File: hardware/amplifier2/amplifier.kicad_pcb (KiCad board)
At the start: 2 copper layers, 95 x 82 mm, 132 parts, among them IC1 AD8331, IC2 ISL55210, IC3 LP38798, IC4 NC7SVU04, IC5 LTC2252, J1 0, M1 MountingHole_3.2mm_M3_Pad, M2 MountingHole_3.2mm_M3_Pad, M3 MountingHole_3.2mm_M3_Pad, M4 MountingHole_3.2mm_M3_Pad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

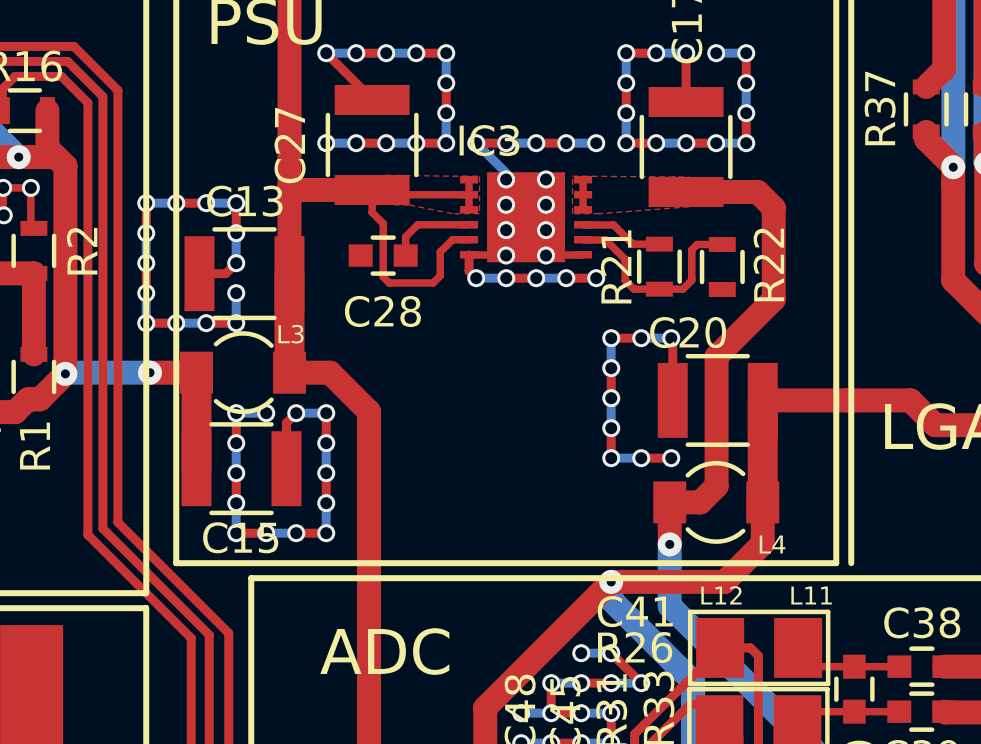
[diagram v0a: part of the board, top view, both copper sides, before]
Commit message: fixed wrong footprint
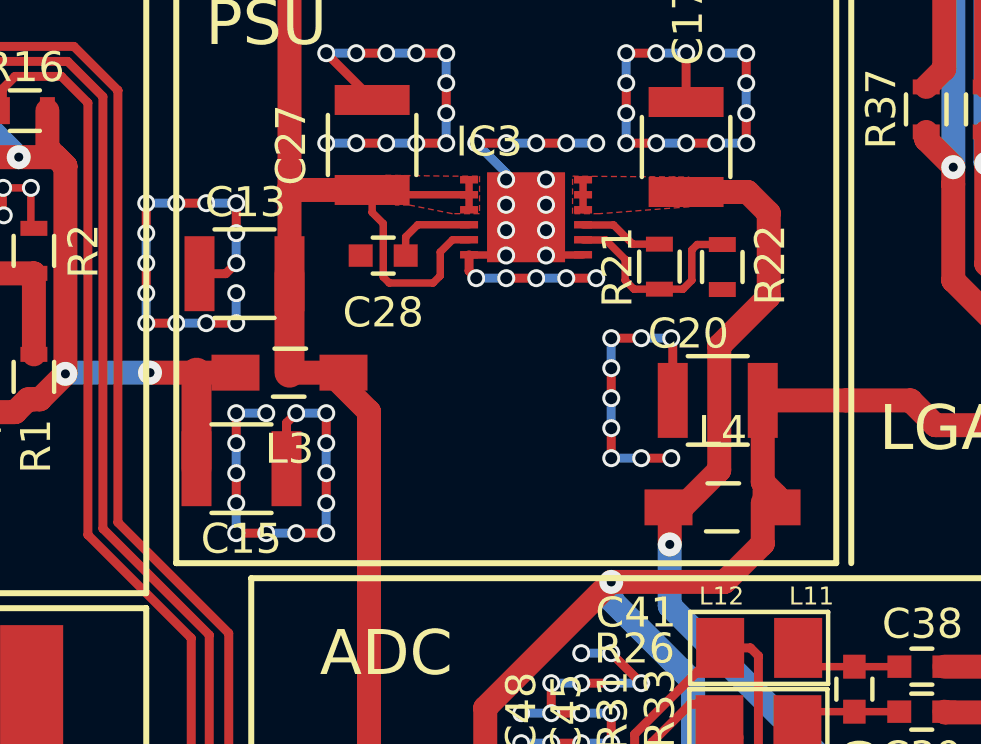
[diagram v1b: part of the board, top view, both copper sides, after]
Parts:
- L3, L4: footprint SDRfootprints:COIL_445-4177-1-ND -> Choke_SMD:Choke_SMD_1206_Standard
- moved L4 1.77 mm to (154.2, 88.1)
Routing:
- net +5VA: track 55.9 -> 57.2 mm
- net +3V3: track 113.6 -> 112.9 mm
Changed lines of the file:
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@@
   (general
     (links 296)
-    (no_connects 2)
-    (area 54 23.919999 210.580001 153.745)
+    (no_connects 5)
+    (area 94.924999 47.924999 190.075001 130.075001)
     (thickness 1.6)
     (drawings 51)
-    (tracks 1415)
+    (tracks 1418)
     (zones 0)
     (modules 132)
@@
   )
   (setup
-    (last_trace_width 0.25)
+    (last_trace_width 0.8)
     (user_trace_width 0.3)
     (user_trace_width 0.8)
@@
     )
   )
-  (module SDRfootprints:COIL_445-4177-1-ND (layer F.Cu)
-    (at 139.775 83.65 180)
-    (fp_text reference L3 (at -0.045 1.26 180) (layer F.SilkS)
-      (effects (font (size 0.6 0.6) (thickness 0.12)))
-    )
-    (fp_text value 22u (at 1.55 1.9 180) (layer F.Fab)
-      (effects (font (size 0.6 0.6) (thickness 0.12)))
-    )
-    (fp_arc (start 1.55 0) (end 0.6 -0.9) (angle 90) (layer F.SilkS) (width 0.15))
-    (fp_arc (start 1.55 0) (end 2.45 0.95) (angle 90) (layer F.SilkS) (width 0.15))
-    (pad 2 smd rect (at 3.1 0 180) (size 1.1 1.4) (layers F.Cu F.Paste F.Mask)
-      (net 4 +5VA))
-    (pad 1 smd rect (at 0 0 180) (size 1.1 1.4) (layers F.Cu F.Paste F.Mask)
-      (net 3 +5V))
-  )
-  (module SDRfootprints:COIL_445-4177-1-ND (layer F.Cu)
-    (at 152.45 87.975)
-    (fp_text reference L4 (at 3.41 1.425) (layer F.SilkS)
-      (effects (font (size 0.6 0.6) (thickness 0.12)))
-    )
-    (fp_text value 22u (at 1.55 1.9) (layer F.Fab)
-      (effects (font (size 0.6 0.6) (thickness 0.12)))
-    )
-    (fp_arc (start 1.55 0) (end 0.6 -0.9) (angle 90) (layer F.SilkS) (width 0.15))
-    (fp_arc (start 1.55 0) (end 2.45 0.95) (angle 90) (layer F.SilkS) (width 0.15))
-    (pad 2 smd rect (at 3.1 0) (size 1.1 1.4) (layers F.Cu F.Paste F.Mask)
-      (net 6 +3.3VADC))
-    (pad 1 smd rect (at 0 0) (size 1.1 1.4) (layers F.Cu F.Paste F.Mask)
-      (net 5 +3V3))
-  )
   (module Resistors_SMD:R_0603 (layer F.Cu)
     (at 168.605 86.075)
@@
       (net 117 "Net-(T4-Pad1)"))
   )
+  (module Choke_SMD:Choke_SMD_1206_Standard (layer F.Cu)
+    (at 139.775 83.65 180)
+    (descr "Choke, Drossel, SMD, 1206, Standard,")
+    (tags "Choke, Drossel, SMD, 1206, Standard,")
+    (attr smd)
+    (fp_text reference L3 (at 0 -2.54 180) (layer F.SilkS)
+      (effects (font (size 1 1) (thickness 0.15)))
+    )
+    (fp_text value 22u (at 0 2.54 180) (layer F.Fab)
+      (effects (font (size 1 1) (thickness 0.15)))
+    )
+    (fp_circle (center 0 0) (end 0.39878 0) (layer F.Adhes) (width 0.381))
+    (fp_circle (center 0 0) (end 0.20066 -0.0508) (layer F.Adhes) (width 0.381))
+    (fp_line (start -0.55118 0.8001) (end 0.50038 0.8001) (layer F.SilkS) (width 0.15))
+    (fp_line (start 0.55118 -0.8001) (end -0.50038 -0.8001) (layer F.SilkS) (width 0.15))
+    (pad 1 smd rect (at -1.80086 0 180) (size 1.6002 1.19888) (layers F.Cu F.Paste F.Mask)
+      (net 3 +5V))
+    (pad 2 smd rect (at 1.80086 0 180) (size 1.6002 1.19888) (layers F.Cu F.Paste F.Mask)
+      (net 4 +5VA))
+  )
+  (module Choke_SMD:Choke_SMD_1206_Standard (layer F.Cu)
+    (at 154.21 88.14)
+    (descr "Choke, Drossel, SMD, 1206, Standard,")
+    (tags "Choke, Drossel, SMD, 1206, Standard,")
+    (attr smd)
+    (fp_text reference L4 (at 0 -2.54) (layer F.SilkS)
+      (effects (font (size 1 1) (thickness 0.15)))
+    )
+    (fp_text value 22u (at 0 2.54) (layer F.Fab)
+      (effects (font (size 1 1) (thickness 0.15)))
+    )
+    (fp_line (start 0.55118 -0.8001) (end -0.50038 -0.8001) (layer F.SilkS) (width 0.15))
+    (fp_line (start -0.55118 0.8001) (end 0.50038 0.8001) (layer F.SilkS) (width 0.15))
+    (fp_circle (center 0 0) (end 0.20066 -0.0508) (layer F.Adhes) (width 0.381))
+    (fp_circle (center 0 0) (end 0.39878 0) (layer F.Adhes) (width 0.381))
+    (pad 2 smd rect (at 1.80086 0) (size 1.6002 1.19888) (layers F.Cu F.Paste F.Mask)
+      (net 6 +3.3VADC))
+    (pad 1 smd rect (at -1.80086 0) (size 1.6002 1.19888) (layers F.Cu F.Paste F.Mask)
+      (net 5 +3V3))
+  )
   (dimension 82 (width 0.3) (layer Dwgs.User)
     (gr_text "82.000 mm" (at 60.65 89 90) (layer Dwgs.User)
@@
   (via (at 138.7 110.275) (size 0.8) (drill 0.3) (layers F.Cu B.Cu) (net 3))
   (segment (start 139.775 80.35) (end 139.775 83.65) (width 1) (layer F.Cu) (net 3) (status 30))
+  (segment (start 136.675 83.65) (end 137.97414 83.65) (width 0.8) (layer F.Cu) (net 4))
   (segment (start 135.125 83.65) (end 132.345 83.65) (width 0.8) (layer B.Cu) (net 4))
   (segment (start 132.345 83.65) (end 132.305001 83.689999) (width 0.8) (layer B.Cu) (net 4))
@@
   (segment (start 136.675 83.65) (end 136.675 86.85) (width 1) (layer F.Cu) (net 4) (status 30))
   (segment (start 127.105 83.84) (end 127.105 85.74) (width 0.8) (layer F.Cu) (net 4) (status 30))
+  (segment (start 152.45 89.375) (end 152.45 88.18086) (width 0.8) (layer F.Cu) (net 5))
+  (segment (start 152.45 88.18086) (end 152.40914 88.14) (width 0.8) (layer F.Cu) (net 5))
+  (via (at 152.45 89.375) (size 0.8) (drill 0.3) (layers F.Cu B.Cu) (net 5))
+  (segment (start 152.995 77.6275) (end 155.045 77.6275) (width 0.8) (layer F.Cu) (net 5))
+  (segment (start 155.045 77.6275) (end 155.75 78.3325) (width 0.8) (layer F.Cu) (net 5))
+  (segment (start 155.75 78.3325) (end 155.75 81.109502) (width 0.8) (layer F.Cu) (net 5))
+  (segment (start 155.75 81.109502) (end 154.1 82.759502) (width 0.8) (layer F.Cu) (net 5))
+  (segment (start 154.1 82.759502) (end 154.1 86.9) (width 0.8) (layer F.Cu) (net 5))
+  (segment (start 154.1 86.9) (end 152.86 88.14) (width 0.8) (layer F.Cu) (net 5))
+  (segment (start 152.86 88.14) (end 152.40914 88.14) (width 0.8) (layer F.Cu) (net 5))
   (segment (start 168.725 118.54) (end 166.54 118.54) (width 0.8) (layer F.Cu) (net 5))
   (segment (start 114.625 121.7) (end 135.545 121.7) (width 0.3) (layer B.Cu) (net 5))
@@
   (segment (start 149.56 77.22) (end 149.56 77.72) (width 0.25) (layer F.Cu) (net 5))
   (segment (start 152.6535 77.969) (end 152.995 77.6275) (width 0.25) (layer F.Cu) (net 5))
-  (segment (start 154.011 87.4305) (end 154.011 83.1125) (width 0.8) (layer F.Cu) (net 5))
-  (segment (start 154.011 83.1125) (end 155.916 81.2075) (width 0.8) (layer F.Cu) (net 5))
-  (segment (start 155.916 81.2075) (end 155.916 78.1595) (width 0.8) (layer F.Cu) (net 5))
-  (segment (start 155.916 78.1595) (end 155.384 77.6275) (width 0.8) (layer F.Cu) (net 5))
-  (segment (start 155.384 77.6275) (end 152.995 77.6275) (width 0.8) (layer F.Cu) (net 5))
-  (segment (start 153.4665 87.975) (end 154.011 87.4305) (width 0.8) (layer F.Cu) (net 5))
-  (segment (start 152.45 87.975) (end 153.4665 87.975) (width 0.8) (layer F.Cu) (net 5))
   (segment (start 152.5945 77.227) (end 152.995 77.6275) (width 0.25) (layer F.Cu) (net 5))
   (segment (start 113.39038 122.93462) (end 114.625 121.7) (width 0.3) (layer B.Cu) (net 5))
@@
   (segment (start 163.805 115.805) (end 166.54 118.54) (width 0.8) (layer F.Cu) (net 5))
   (segment (start 152.45 89.375) (end 152.45 91.425) (width 0.8) (layer B.Cu) (net 5))
-  (segment (start 152.45 91.425) (end 162.3 101.275) (width 0.8) (layer B.Cu) (net 5))
   (segment (start 162.3 101.275) (end 162.3 103.725) (width 0.8) (layer B.Cu) (net 5))
+  (segment (start 152.45 91.425) (end 162.3 101.275) (width 0.8) (layer B.Cu) (net 5))
   (segment (start 162.305 103.73) (end 162.3 103.725) (width 0.8) (layer F.Cu) (net 5))
   (segment (start 162.305 105.23) (end 162.305 103.73) (width 0.8) (layer F.Cu) (net 5))
   (via (at 162.3 103.725) (size 0.8) (drill 0.3) (layers F.Cu B.Cu) (net 5))
-  (segment (start 152.45 87.975) (end 152.45 89.375) (width 0.8) (layer F.Cu) (net 5))
-  (via (at 152.45 89.375) (size 0.8) (drill 0.3) (layers F.Cu B.Cu) (net 5))
-  (segment (start 152.425 88) (end 152.45 87.975) (width 0.8) (layer F.Cu) (net 5))
   (segment (start 163.806617 110.989951) (end 163.806617 110.219953) (width 0.3) (layer F.Cu) (net 5))
   (segment (start 163.806617 110.219953) (end 162.306617 108.719953) (width 0.3) (layer F.Cu) (net 5))
@@
   (segment (start 148.955 107.825) (end 148.955 108.675) (width 0.25) (layer F.Cu) (net 5))
   (segment (start 148.955 108.675) (end 148.705 108.925) (width 0.25) (layer F.Cu) (net 5))
+  (segment (start 156.01086 87.76086) (end 155.55 87.3) (width 0.8) (layer F.Cu) (net 6))
+  (segment (start 155.55 87.3) (end 155.55 84.575) (width 0.8) (layer F.Cu) (net 6))
+  (segment (start 156.01086 88.14) (end 156.01086 87.76086) (width 0.8) (layer F.Cu) (net 6))
   (segment (start 165.65 85.25) (end 165.5 85.4) (width 0.8) (layer F.Cu) (net 6))
   (segment (start 165.5 85.4) (end 161.3 85.4) (width 0.8) (layer F.Cu) (net 6))
@@
   (segment (start 151.105 103.675) (end 151.28 103.675) (width 0.25) (layer F.Cu) (net 6))
   (segment (start 170.705 86.325) (end 170.905 86.325) (width 0.25) (layer F.Cu) (net 6) (status 30))
-  (segment (start 155.55 87.975) (end 155.55 84.575) (width 1) (layer F.Cu) (net 6) (status 30))
   (segment (start 140.667902 120.250022) (end 136.824999 116.407119) (width 0.3) (layer B.Cu) (net 7))
   (segment (start 137.450011 112.874999) (end 137.75001 112.575) (width 0.3) (layer B.Cu) (net 7))
@@
     (min_thickness 0.254)
     (keepout (tracks not_allowed) (vias not_allowed) (copperpour not_allowed))
-    (fill (arc_segments 16) (thermal_gap 0) (thermal_bridge_width 0.508))
+    (fill yes (arc_segments 16) (thermal_gap 0) (thermal_bridge_width 0.508))
     (polygon
       (pts
